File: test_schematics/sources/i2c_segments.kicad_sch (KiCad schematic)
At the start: 29 parts, among them J401 Conn_01x03_Pin, Q401 BSS138, Q402 BSS138, Q403 BSS138, Q404 BSS138, U401 STM32F030F4Px, U402 PCA9536DP, U403 PCA9536DP, U404 PCA9306, U405 PCA9536DP, U406 PCA9536DP, U407 PCA9536DP, U408 PCA9536DP

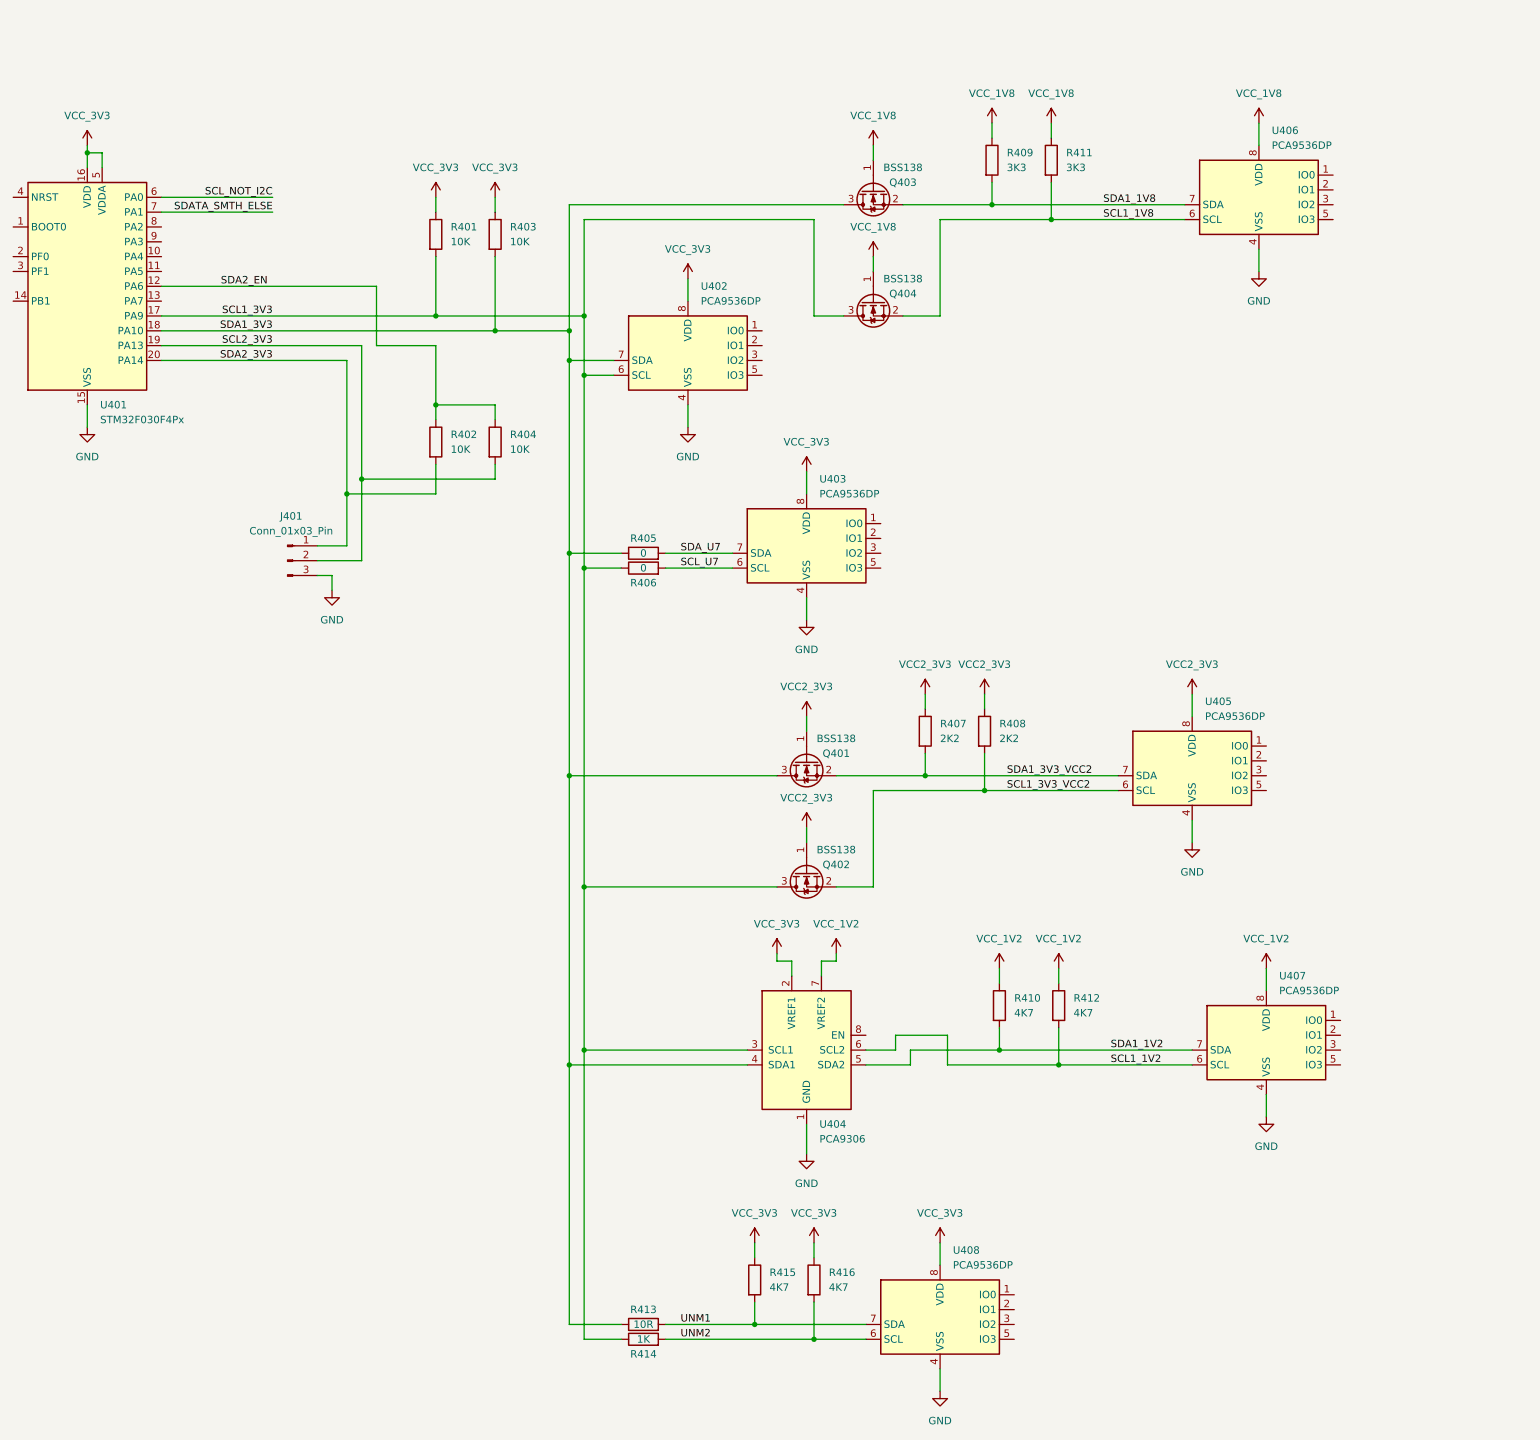
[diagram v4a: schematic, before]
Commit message: feat: identify I2C direct and common segments, check for missing pull-ups or pull-ups to nowhere, identify voltage translators.
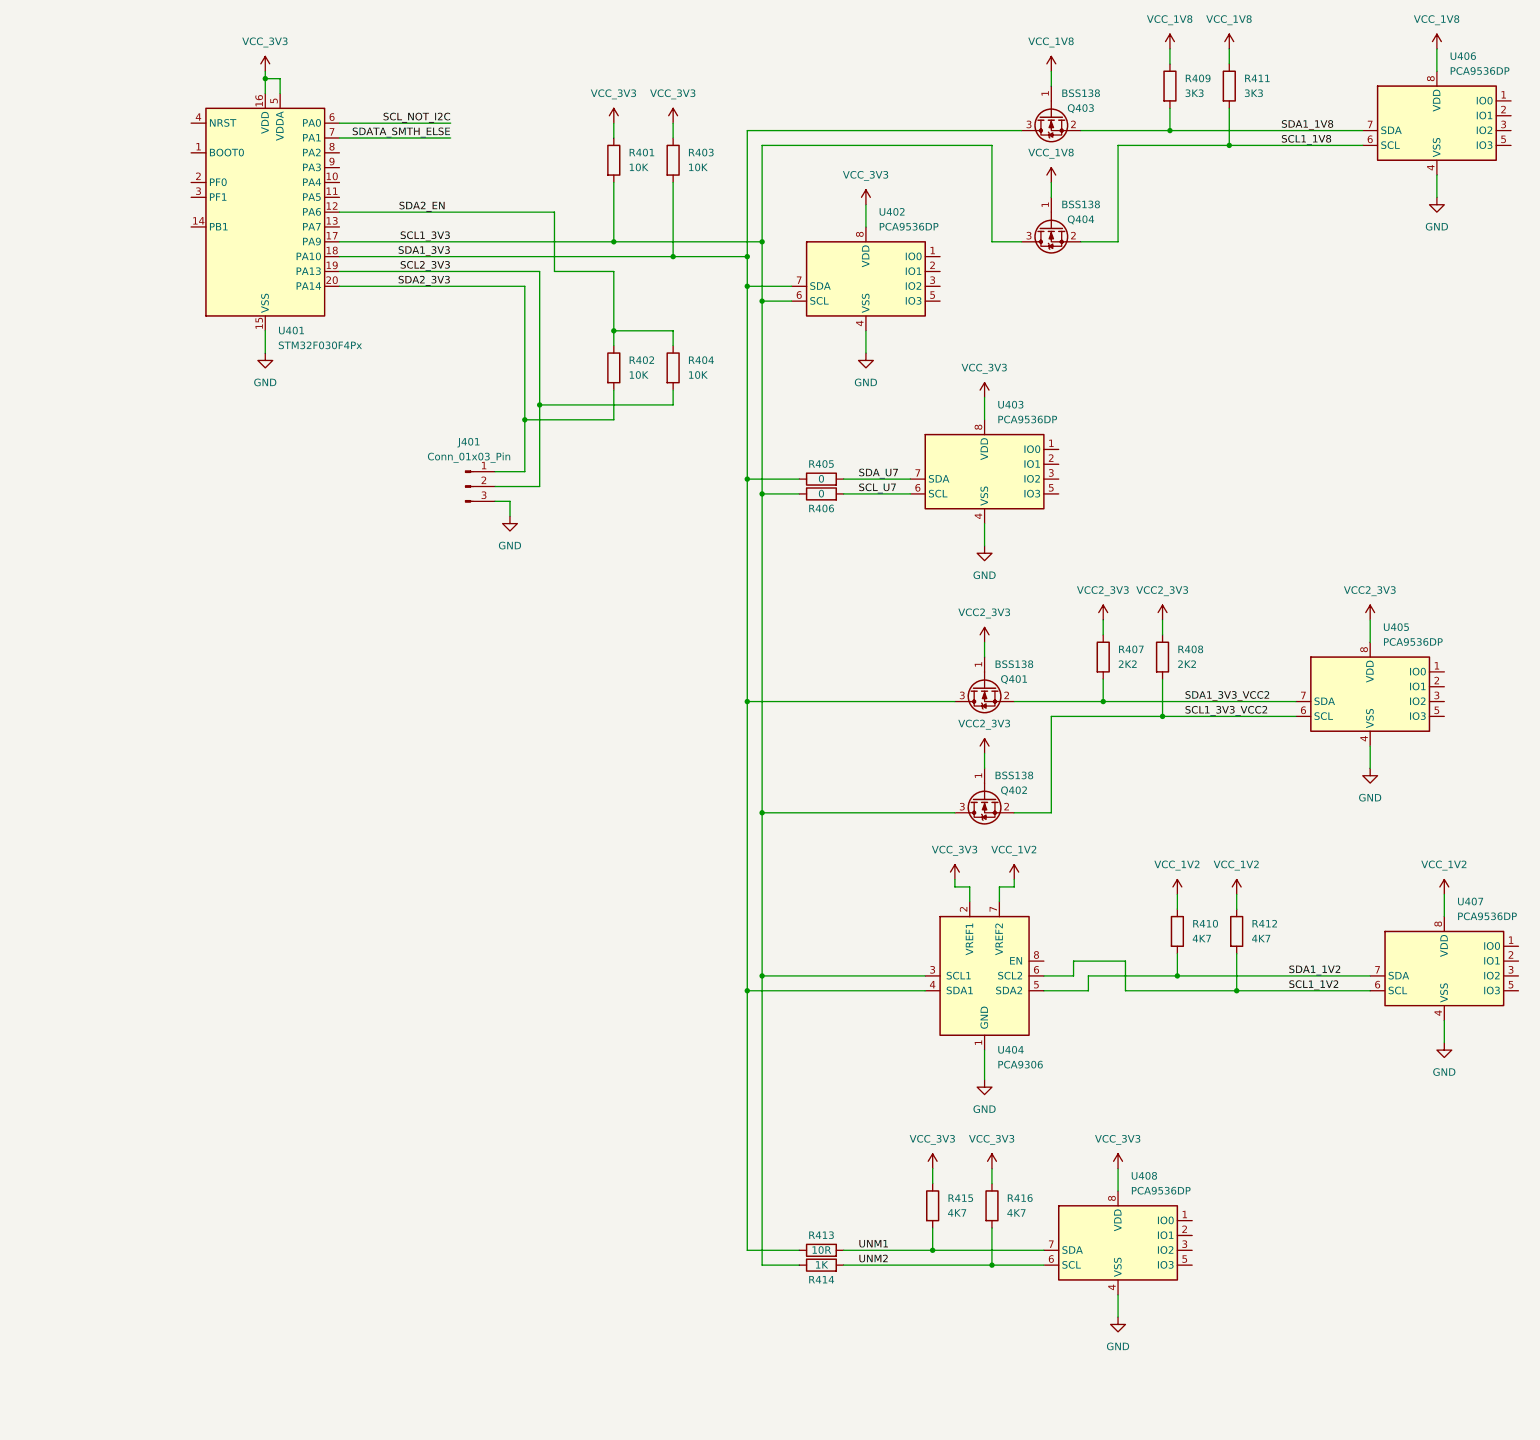
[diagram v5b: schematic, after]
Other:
- moved on the sheet: J401, Q401, Q402, Q403, Q404, R401, R402, R403, R404, R405, R406, R407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
